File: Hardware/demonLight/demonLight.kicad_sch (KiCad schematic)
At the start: 5 parts, among them J1 CONN_IN, J2 CONN_IN

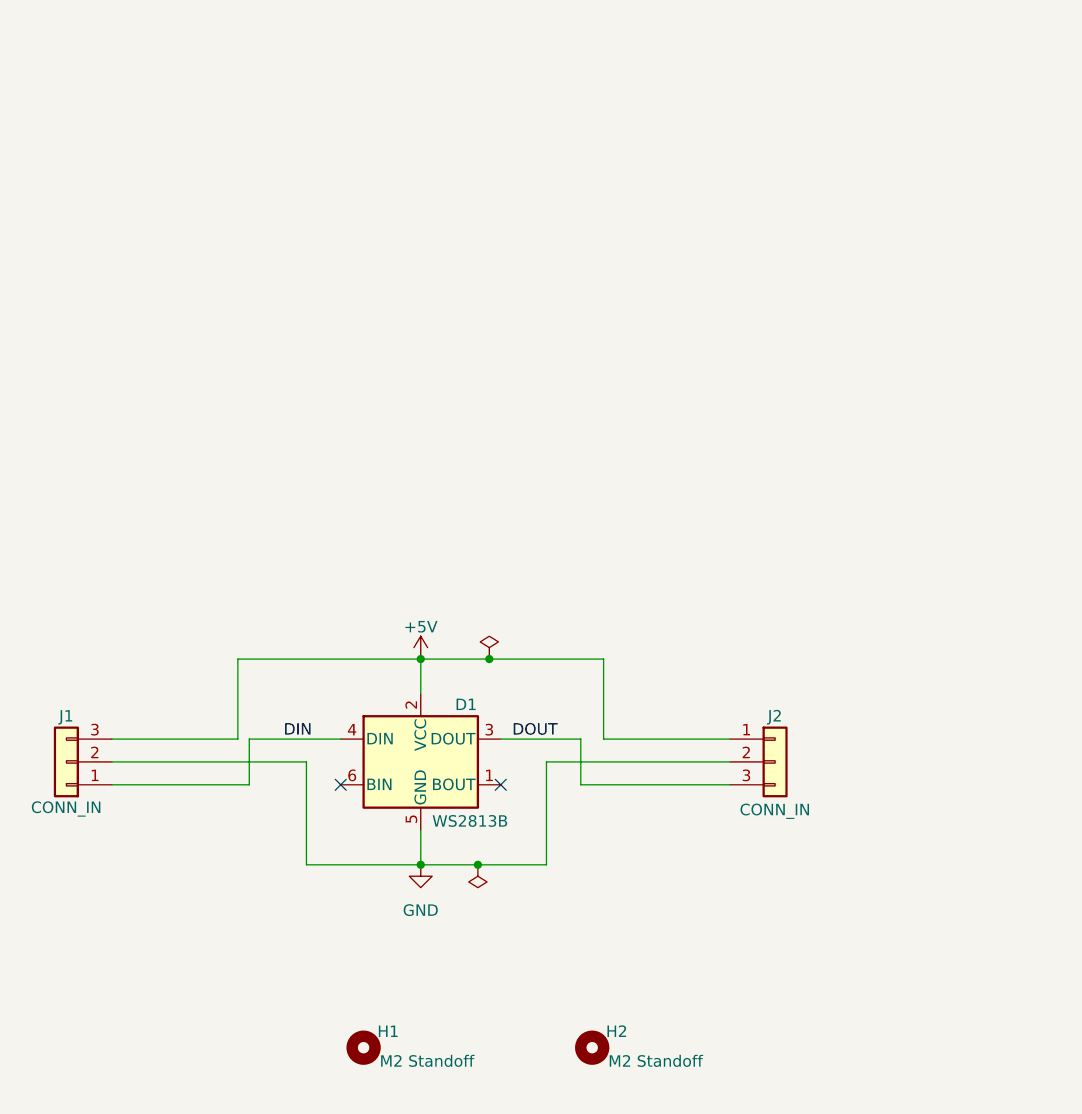
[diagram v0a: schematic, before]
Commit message: doc: Add schematic pdf
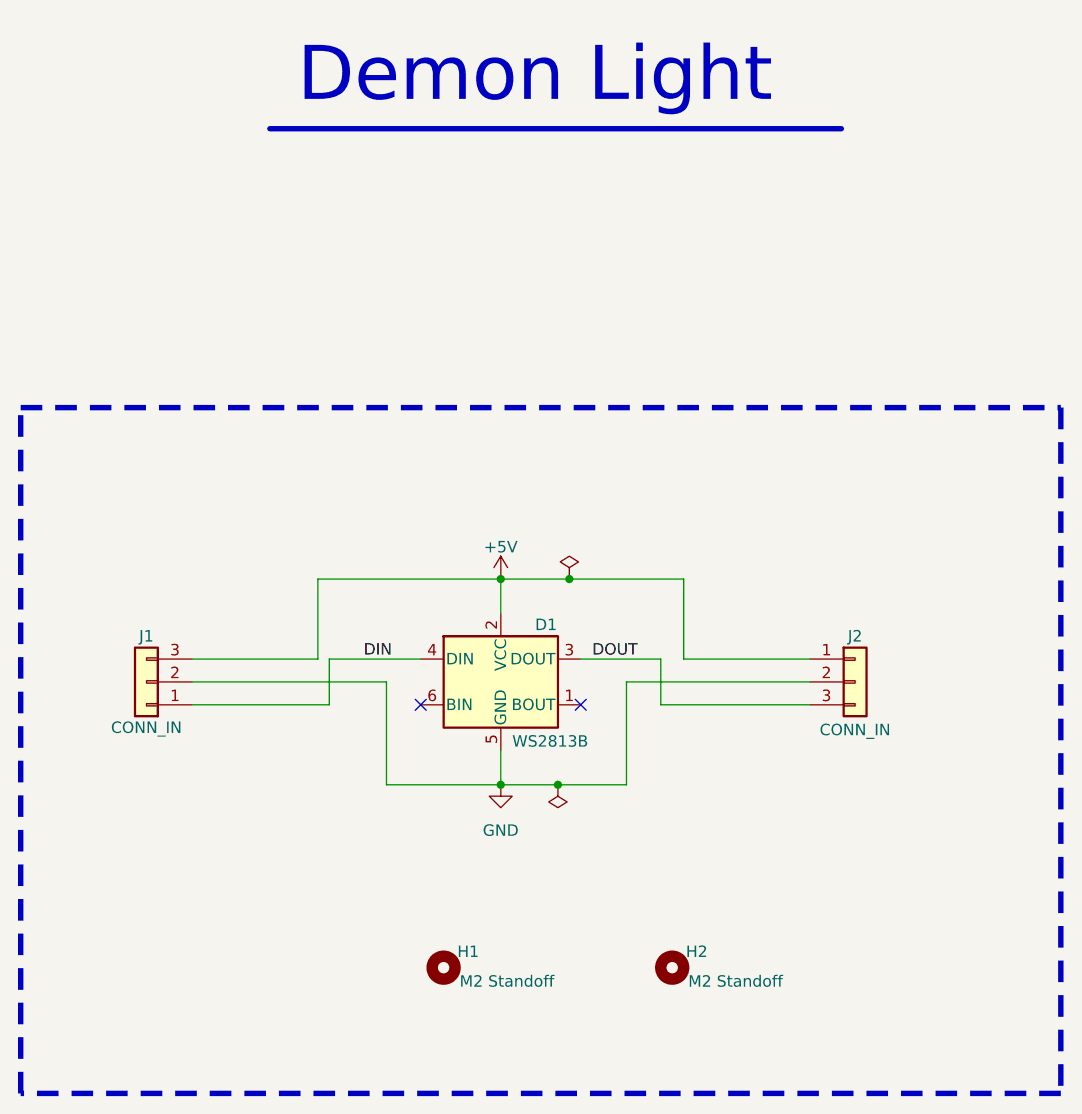
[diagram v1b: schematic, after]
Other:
- note added: "Demon Light"
- title: (none) -> Demon Light
- moved on the sheet: D1, H1, H2, J1, J2
